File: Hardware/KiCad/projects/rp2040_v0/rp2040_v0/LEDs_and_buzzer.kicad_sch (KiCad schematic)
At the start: 13 parts, among them J29 Conn_01x01, Q1 2N7002

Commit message: Fix some wrong schematic footprints.
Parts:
- J29: footprint Connector_PinHeader_2.54mm:PinHeader_1x03_P2.54mm_Vertical -> Connector_PinHeader_2.54mm:PinHeader_1x01_P2.54mm_Vertical
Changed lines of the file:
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@@
       (effects (font (size 1.27 1.27)) (justify left))
     )
-    (property "Footprint" "Connector_PinHeader_2.54mm:PinHeader_1x03_P2.54mm_Vertical" (id 2) (at 119.38 73.66 0)
+    (property "Footprint" "Connector_PinHeader_2.54mm:PinHeader_1x01_P2.54mm_Vertical" (id 2) (at 119.38 73.66 0)
       (effects (font (size 1.27 1.27)) hide)
     )

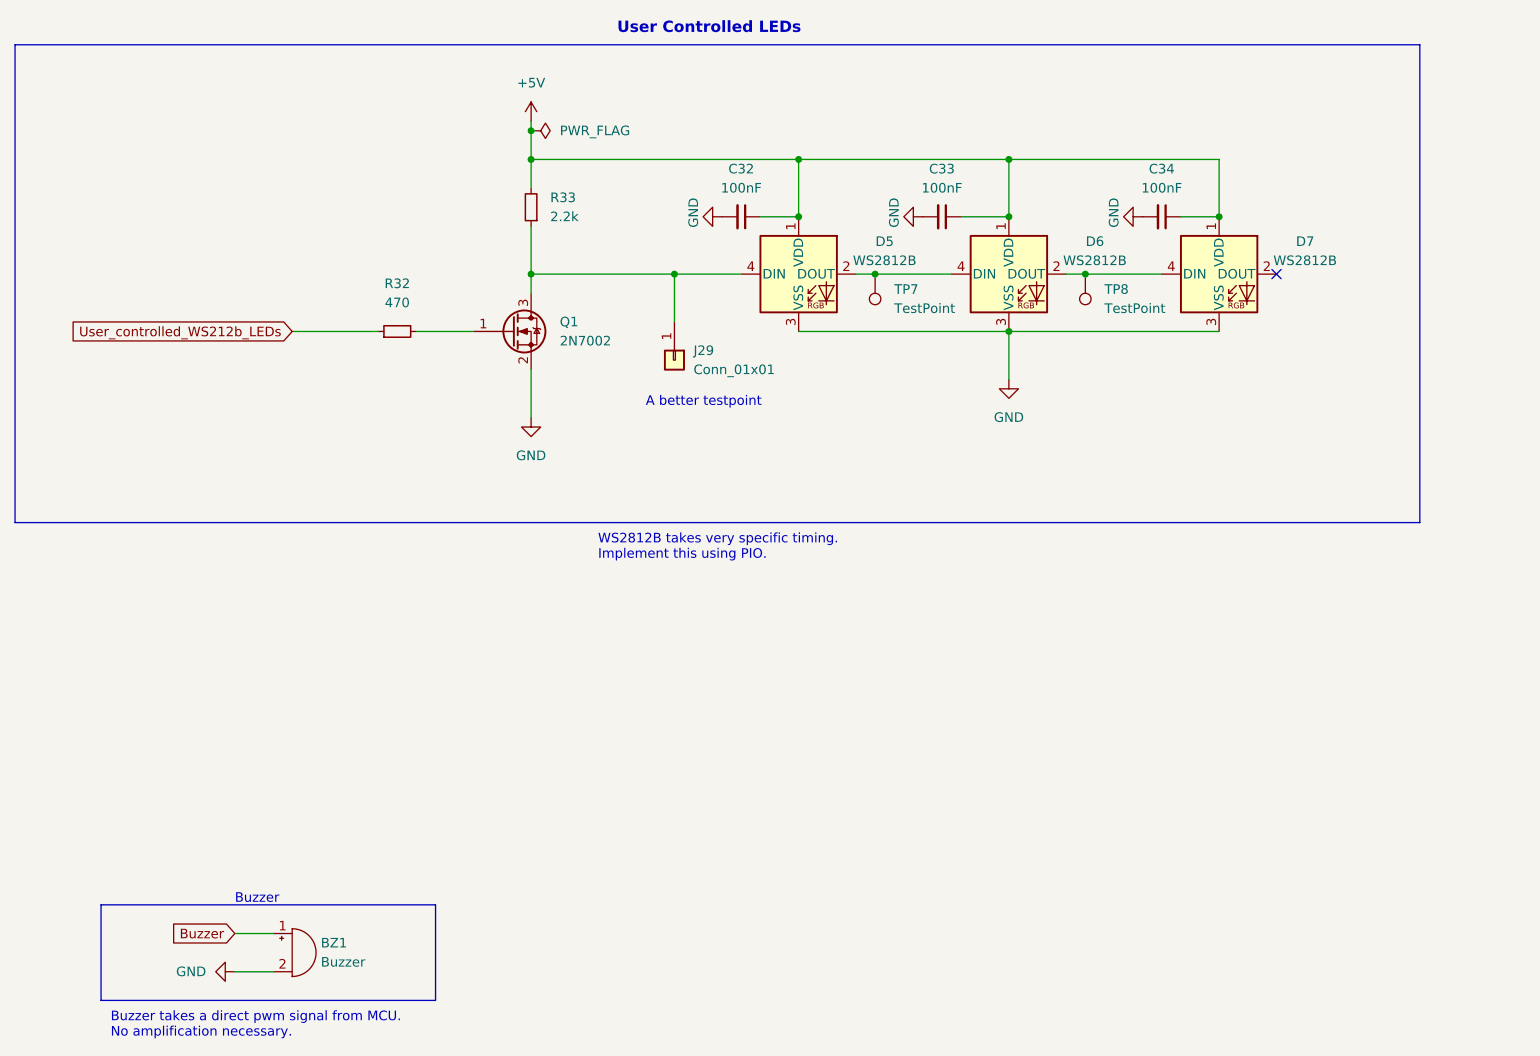
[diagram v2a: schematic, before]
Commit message: Swap out ws2812b led for small red and green led.
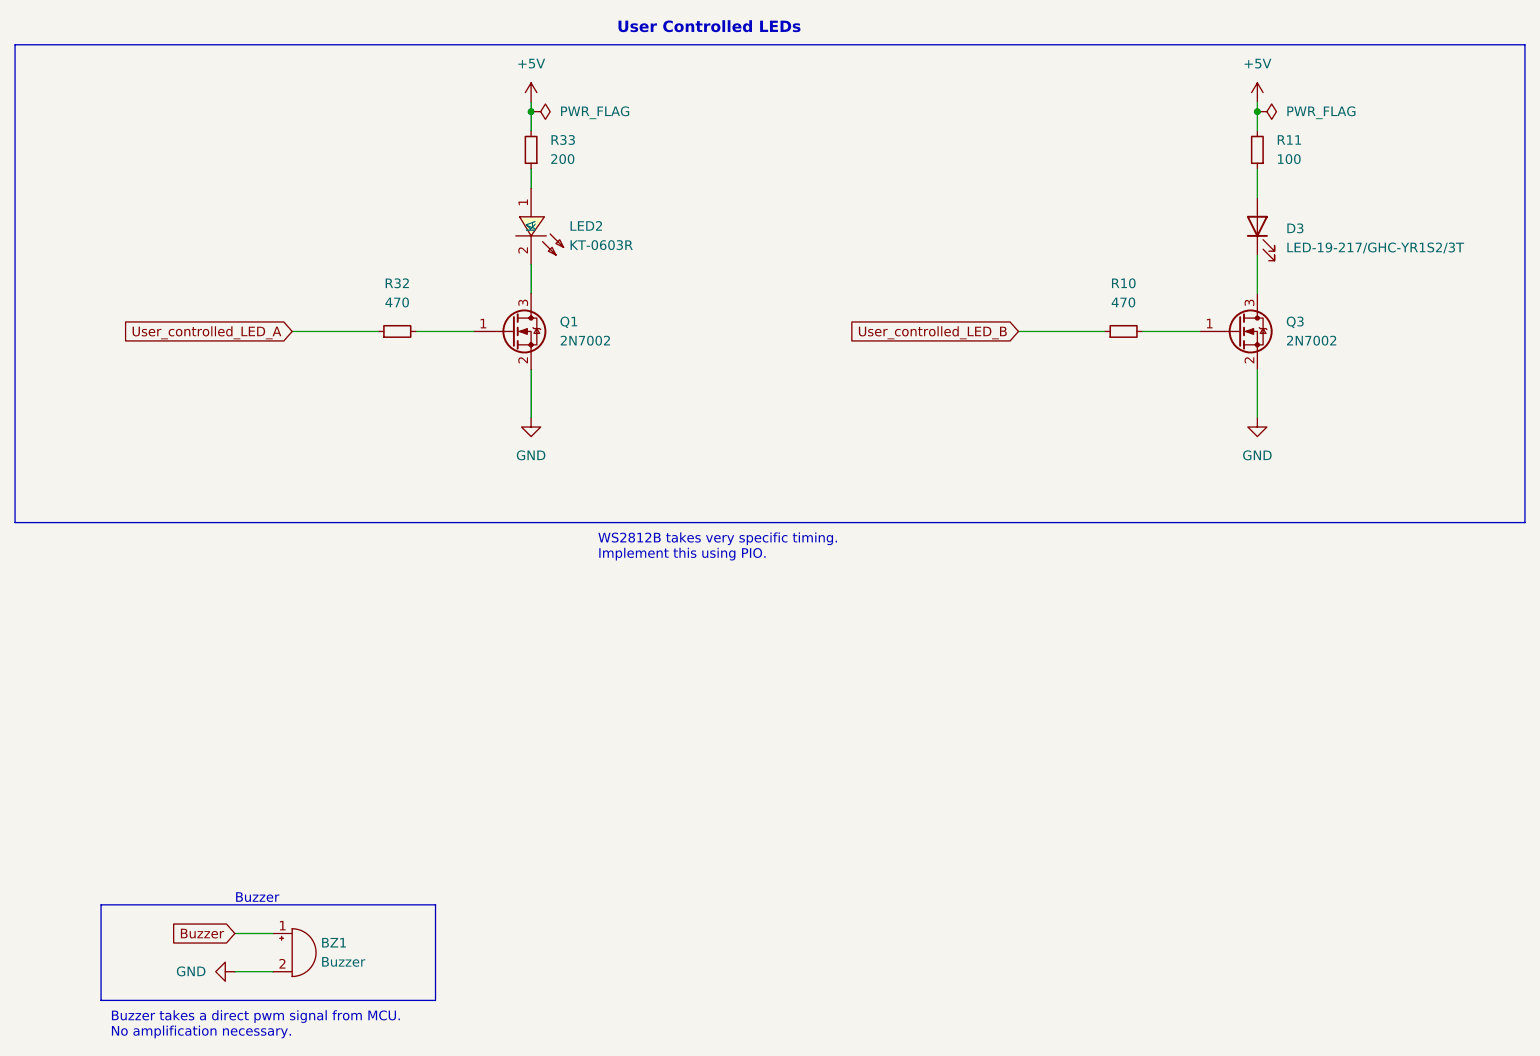
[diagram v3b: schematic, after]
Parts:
- removed C32, C33, C34: 100nF, Capacitor_SMD:C_0402_1005Metric, symbol Device:C_Small
- removed D5, D6, D7: WS2812B, LED_SMD:LED_WS2812B_PLCC4_5.0x5.0mm_P3.2mm, symbol LED:WS2812B
- removed J29: Conn_01x01, Connector_PinHeader_2.54mm:PinHeader_1x01_P2.54mm_Vertical, symbol Connector_Generic:Conn_01x01
- removed TP7, TP8: TestPoint, TestPoint:TestPoint_Pad_1.0x1.0mm, symbol Connector:TestPoint
- added D3: LED-19-217/GHC-YR1S2/3T, easyeda2kicad:LED0603-R-RD, symbol Device:LED
- added LED2: KT-0603R, easyeda2kicad:LED0603-R-RD, symbol easyeda2kicad_flight_computer:KT-0603R
- added Q3: 2N7002, Package_TO_SOT_SMD:SOT-23, symbol Transistor_FET:2N7002
- added R10: 470, Resistor_SMD:R_0402_1005Metric, symbol Device:R_Small
- added R11: 100, Resistor_SMD:R_0402_1005Metric, symbol Device:R_Small
- R33: value 2.2k -> 200
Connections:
- net +5V: now also R11.2
- net GND: now also Q3.2 (S)
- net at Q1.3 (D): now also LED2.2 (K); no longer R33.1
- net User_controlled_WS212b_LEDs renamed User_controlled_LED_A
- new net: D3.1 (K), Q3.3 (D)
- new net: D3.2 (A), R11.1
- new net: LED2.1 (A), R33.1
- new net: Q3.1 (G), R10.2
- new net User_controlled_LED_B: R10.1
- no-connect marks 1 -> 0
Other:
- note removed: "A better testpoint"
- moved on the sheet: R33

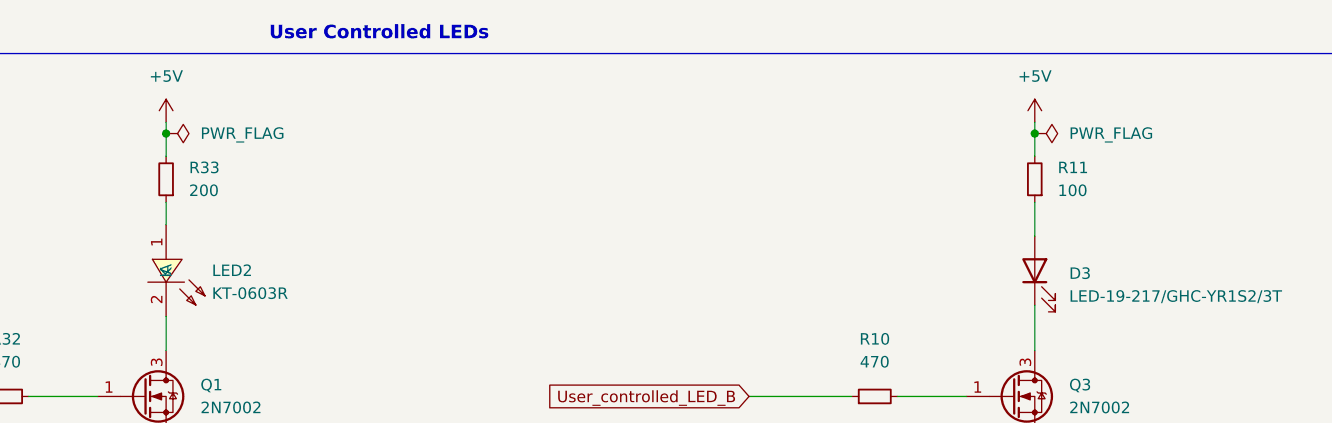
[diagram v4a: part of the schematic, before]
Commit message: Remove reaction wheel LDO. Add jumper to select power source.
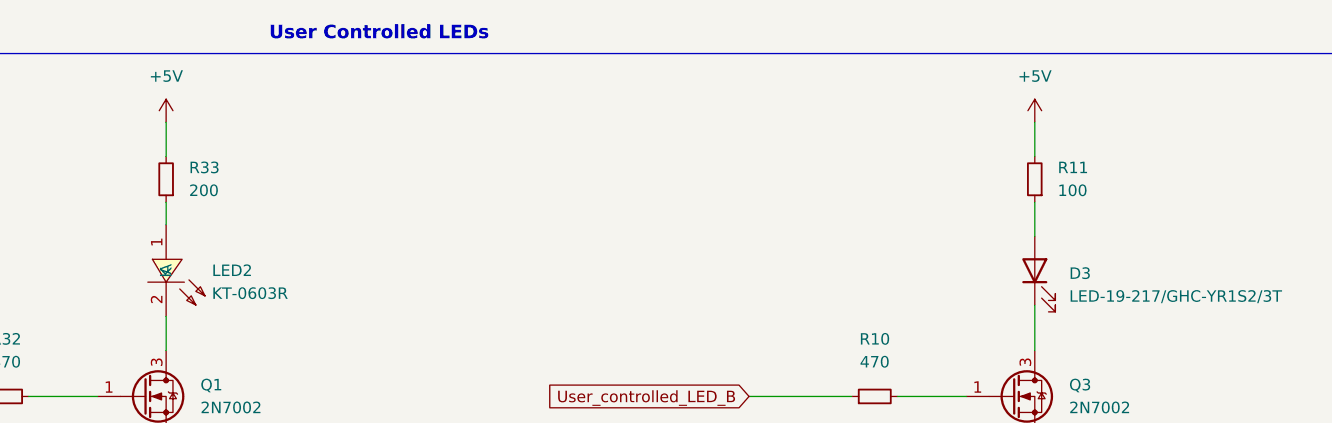
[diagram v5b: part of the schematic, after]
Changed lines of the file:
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@@
     (rev "v0.1")
   )
-  (junction (at 196.85 40.64) (diameter 0) (color 0 0 0 0)
-  )
-  (junction (at 100.33 40.64) (diameter 0) (color 0 0 0 0)
-  )
   (wire (pts (xy 165.1 69.85) (xy 176.53 69.85))
     (stroke (width 0) (type default) (color 0 0 0 0))
@@
     (stroke (width 0) (type default) (color 0 0 0 0))
   )
-  (wire (pts (xy 196.85 39.37) (xy 196.85 40.64))
+  (wire (pts (xy 196.85 39.37) (xy 196.85 43.18))
     (stroke (width 0) (type default) (color 0 0 0 0))
   )
@@
     (stroke (width 0) (type default) (color 0 0 0 0))
   )
-  (wire (pts (xy 100.33 39.37) (xy 100.33 40.64))
+  (wire (pts (xy 100.33 39.37) (xy 100.33 43.18))
     (stroke (width 0) (type default) (color 0 0 0 0))
   )
@@
     (stroke (width 0) (type default) (color 0 0 0 0))
   )
-  (wire (pts (xy 196.85 40.64) (xy 196.85 43.18))
-    (stroke (width 0) (type default) (color 0 0 0 0))
-  )
   (polyline (pts (xy 87.63 146.05) (xy 87.63 158.75))
     (stroke (width 0) (type default) (color 0 0 0 0))
   )
   (polyline (pts (xy 87.63 158.75) (xy 43.18 158.75))
-    (stroke (width 0) (type default) (color 0 0 0 0))
-  )
-  (wire (pts (xy 100.33 40.64) (xy 100.33 43.18))
     (stroke (width 0) (type default) (color 0 0 0 0))
   )
@@
     (pin "3")
   )
-  (symbol (lib_id "power:PWR_FLAG") (at 196.85 40.64 270) (unit 1)
-    (in_bom yes) (on_board yes) (fields_autoplaced)
-    (property "Reference" "#FLG0101" (id 0) (at 198.755 40.64 0)
-      (effects (font (size 1.27 1.27)) hide)
-    )
-    (property "Value" "PWR_FLAG" (id 1) (at 200.66 40.6399 90)
-      (effects (font (size 1.27 1.27)) (justify left))
-    )
-    (property "Footprint" "" (id 2) (at 196.85 40.64 0)
-      (effects (font (size 1.27 1.27)) hide)
-    )
-    (property "Datasheet" "~" (id 3) (at 196.85 40.64 0)
-      (effects (font (size 1.27 1.27)) hide)
-    )
-    (pin "1")
-  )
   (symbol (lib_id "power:GND") (at 196.85 81.28 0) (unit 1)
     (in_bom yes) (on_board yes) (fields_autoplaced)
@@
     (pin "2")
   )
-  (symbol (lib_id "power:PWR_FLAG") (at 100.33 40.64 270) (unit 1)
-    (in_bom yes) (on_board yes) (fields_autoplaced)
-    (property "Reference" "#FLG06" (id 0) (at 102.235 40.64 0)
-      (effects (font (size 1.27 1.27)) hide)
-    )
-    (property "Value" "PWR_FLAG" (id 1) (at 104.14 40.6399 90)
-      (effects (font (size 1.27 1.27)) (justify left))
-    )
-    (property "Footprint" "" (id 2) (at 100.33 40.64 0)
-      (effects (font (size 1.27 1.27)) hide)
-    )
-    (property "Datasheet" "~" (id 3) (at 100.33 40.64 0)
-      (effects (font (size 1.27 1.27)) hide)
-    )
-    (pin "1")
-  )
   (symbol (lib_id "Device:Buzzer") (at 68.58 152.4 0) (unit 1)
